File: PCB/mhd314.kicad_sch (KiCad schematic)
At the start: 35 parts, among them J1 Raspberry_Pi_2_3, J2 AudioJack_Pentaconn, J4 AudioJack3_SwitchTR, SW1 SW_Push

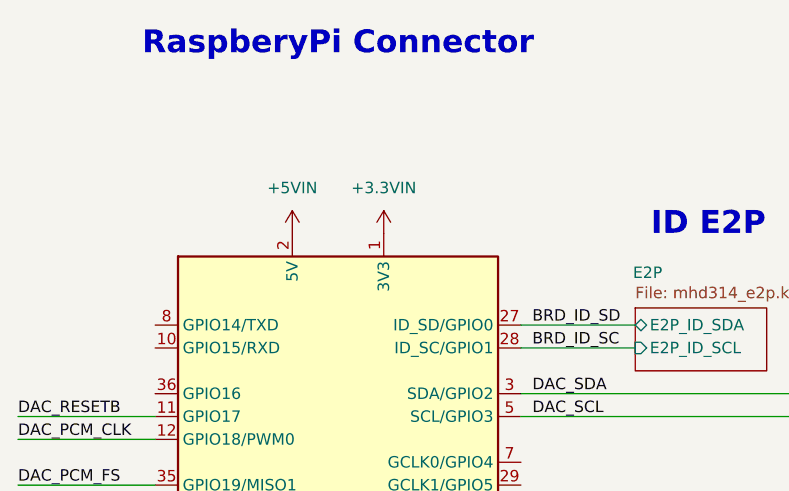
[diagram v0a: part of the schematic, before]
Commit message: Basic routing finished. Still missing some optimizing steps and DRC
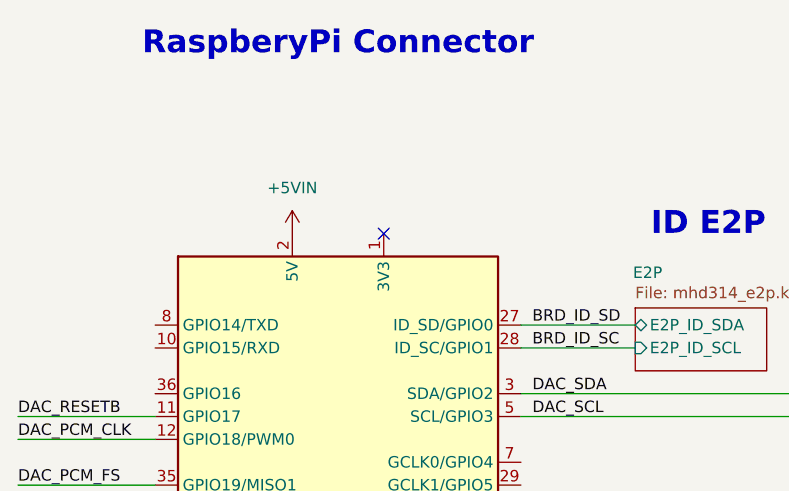
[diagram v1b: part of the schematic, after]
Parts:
- J2: footprint _mahaudio KiCad Library:Jack_4.4mm_Pentaconn_NBA1-24-001_Horizontal -> mahaudio KiCad Library:Jack_4.4mm_Pentaconn_NBA1-24-001_Horizontal; symbol mahaudio_kicad_lib:AudioJack_Pentaconn -> mahaudio KiCad Library:AudioJack_Pentaconn
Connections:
- net +3.3VIN: no longer names the net of J1.1 (3V3), J1.17 (3V3)
- no-connect marks 7 -> 8
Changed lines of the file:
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@@
 	)
 	(no_connect
+		(at 62.23 52.07)
+	)
+	(no_connect
 		(at 254 44.45)
 	)
@@
 	(symbol
 		(lib_id "power:VBUS")
-		(at 62.23 52.07 0)
-		(unit 1)
-		(exclude_from_sim no)
-		(in_bom yes)
-		(on_board yes)
-		(dnp no)
-		(fields_autoplaced yes)
-		(property "Reference" "#PWR083"
-			(at 62.23 55.88 0)
-			(effects
-				(font
-					(size 1.27 1.27)
-				)
-				(hide yes)
-			)
-		)
-		(property "Value" "+3.3VIN"
-			(at 62.23 46.99 0)
-			(effects
-				(font
-					(size 1.27 1.27)
-				)
-			)
-		)
-		(property "Footprint" ""
-			(at 62.23 52.07 0)
-			(effects
-				(font
-					(size 1.27 1.27)
-				)
-				(hide yes)
-			)
-		)
-		(property "Datasheet" ""
-			(at 62.23 52.07 0)
-			(effects
-				(font
-					(size 1.27 1.27)
-				)
-				(hide yes)
-			)
-		)
-		(property "Description" "Power symbol creates a global label with name \"VBUS\""
-			(at 62.23 52.07 0)
-			(effects
-				(font
-					(size 1.27 1.27)
-				)
-				(hide yes)
-			)
-		)
-		(pin "1"
-		)
-		(instances
-			(project "mhd314"
-				(path "/afee45fc-2361-4efb-9cde-757fc2efd57b"
-					(reference "#PWR083")
-					(unit 1)
-				)
-			)
-		)
-	)
-	(symbol
-		(lib_id "power:VBUS")
 		(at 52.07 52.07 0)
 		(unit 1)
@@
 	)
 	(symbol
-		(lib_id "mahaudio_kicad_lib:AudioJack_Pentaconn")
+		(lib_id "mahaudio KiCad Library:AudioJack_Pentaconn")
 		(at 259.08 72.39 180)
 		(unit 1)
@@
 			)
 		)
-		(property "Footprint" "_mahaudio KiCad Library:Jack_4.4mm_Pentaconn_NBA1-24-001_Horizontal"
+		(property "Footprint" "mahaudio KiCad Library:Jack_4.4mm_Pentaconn_NBA1-24-001_Horizontal"
 			(at 263.652 59.436 0)
 			(effects

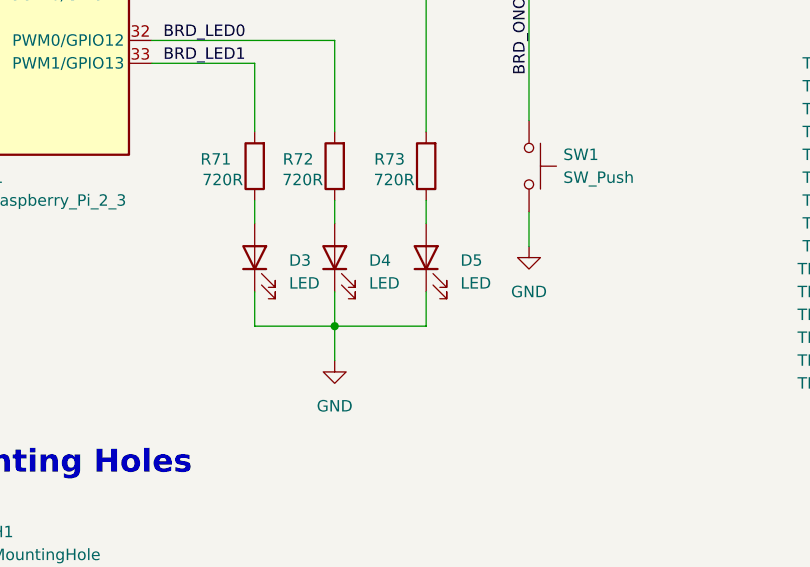
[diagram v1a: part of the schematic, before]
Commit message: Routing revised, added some missing parameters to components
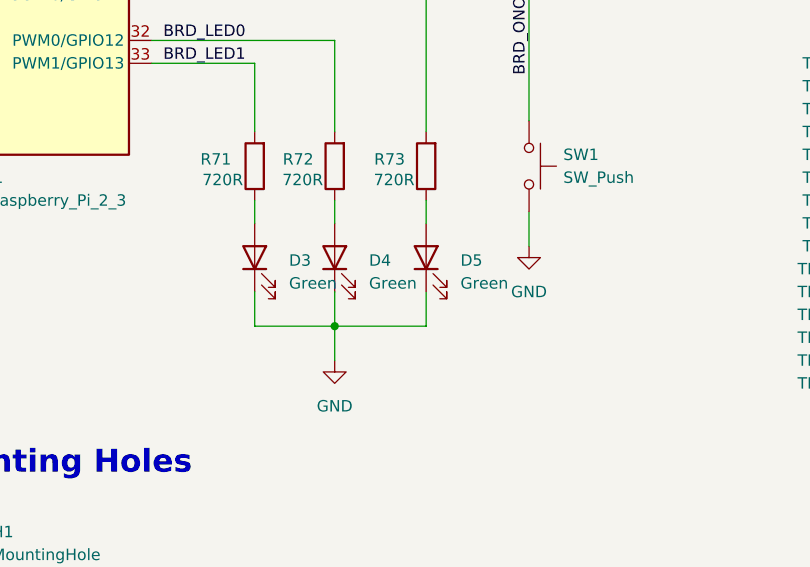
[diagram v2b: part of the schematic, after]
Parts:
- D3, D4, D5: value LED -> Green
- TP1, TP10, TP11, TP12, TP13, TP14, TP15, TP16, TP17, TP18, TP19, TP2, TP20, TP21, TP3, TP4, TP5, TP6, TP7, TP8, TP9: now left out of the parts list
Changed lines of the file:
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@@
 		(unit 1)
 		(exclude_from_sim no)
-		(in_bom yes)
+		(in_bom no)
 		(on_board yes)
 		(dnp no)
@@
 		(unit 1)
 		(exclude_from_sim no)
-		(in_bom yes)
+		(in_bom no)
 		(on_board yes)
 		(dnp no)
@@
 		(unit 1)
 		(exclude_from_sim no)
-		(in_bom yes)
+		(in_bom no)
 		(on_board yes)
 		(dnp no)
@@
 			)
 		)
-		(property "Value" "LED"
+		(property "Value" "Green"
 			(at 111.76 129.8574 90)
 			(effects
@@
 		(unit 1)
 		(exclude_from_sim no)
-		(in_bom yes)
+		(in_bom no)
 		(on_board yes)
 		(dnp no)
@@
 		(unit 1)
 		(exclude_from_sim no)
-		(in_bom yes)
+		(in_bom no)
 		(on_board yes)
 		(dnp no)
@@
 		(unit 1)
 		(exclude_from_sim no)
-		(in_bom yes)
+		(in_bom no)
 		(on_board yes)
 		(dnp no)
@@
 			)
 		)
-		(property "Datasheet" "~"
+		(property "Datasheet" "https://www.sameskydevices.com/product/resource/sj1-353xng.pdf"
 			(at 259.08 52.07 0)
 			(effects
@@
 		(unit 1)
 		(exclude_from_sim no)
-		(in_bom yes)
+		(in_bom no)
 		(on_board yes)
 		(dnp no)
@@
 		(unit 1)
 		(exclude_from_sim no)
-		(in_bom yes)
+		(in_bom no)
 		(on_board yes)
 		(dnp no)
@@
 		(unit 1)
 		(exclude_from_sim no)
-		(in_bom yes)
+		(in_bom no)
 		(on_board yes)
 		(dnp no)
@@
 		(unit 1)
 		(exclude_from_sim no)
-		(in_bom yes)
+		(in_bom no)
 		(on_board yes)
 		(dnp no)
@@
 		(unit 1)
 		(exclude_from_sim no)
-		(in_bom yes)
+		(in_bom no)
 		(on_board yes)
 		(dnp no)
@@
 		(unit 1)
 		(exclude_from_sim no)
-		(in_bom yes)
+		(in_bom no)
 		(on_board yes)
 		(dnp no)
@@
 		(unit 1)
 		(exclude_from_sim no)
-		(in_bom yes)
+		(in_bom no)
 		(on_board yes)
 		(dnp no)
@@
 			)
 		)
-		(property "Value" "LED"
+		(property "Value" "Green"
 			(at 101.6 129.8574 90)
 			(effects
@@
 		(unit 1)
 		(exclude_from_sim no)
-		(in_bom yes)
+		(in_bom no)
 		(on_board yes)
 		(dnp no)
@@
 		(unit 1)
 		(exclude_from_sim no)
-		(in_bom yes)
+		(in_bom no)
 		(on_board yes)
 		(dnp no)
@@
 		(unit 1)
 		(exclude_from_sim no)
-		(in_bom yes)
+		(in_bom no)
 		(on_board yes)
 		(dnp no)
@@
 		(unit 1)
 		(exclude_from_sim no)
-		(in_bom yes)
+		(in_bom no)
 		(on_board yes)
 		(dnp no)
@@
 		(unit 1)
 		(exclude_from_sim no)
-		(in_bom yes)
+		(in_bom no)
 		(on_board yes)
 		(dnp no)
@@
 		(unit 1)
 		(exclude_from_sim no)
-		(in_bom yes)
+		(in_bom no)
 		(on_board yes)
 		(dnp no)
@@
 		(unit 1)
 		(exclude_from_sim no)
-		(in_bom yes)
+		(in_bom no)
 		(on_board yes)
 		(dnp no)
@@
 		(unit 1)
 		(exclude_from_sim no)
-		(in_bom yes)
+		(in_bom no)
 		(on_board yes)
 		(dnp no)
@@
 			)
 		)
-		(property "Value" "LED"
+		(property "Value" "Green"
 			(at 92.71 129.8574 90)
 			(effects

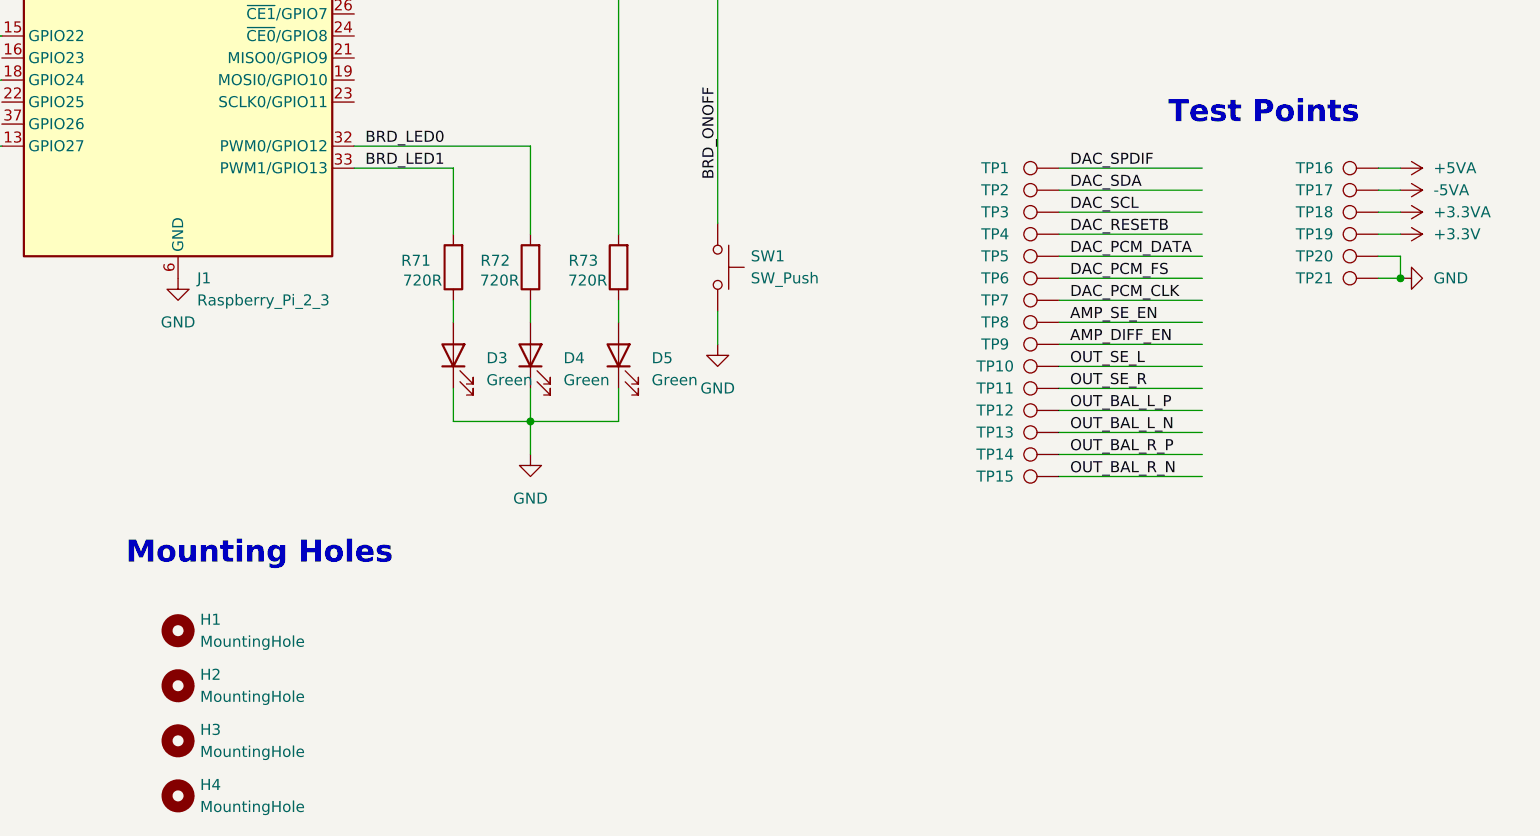
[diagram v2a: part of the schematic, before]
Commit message: Updated PCB with digital traxce suggestions. Added JLCPCB Pns
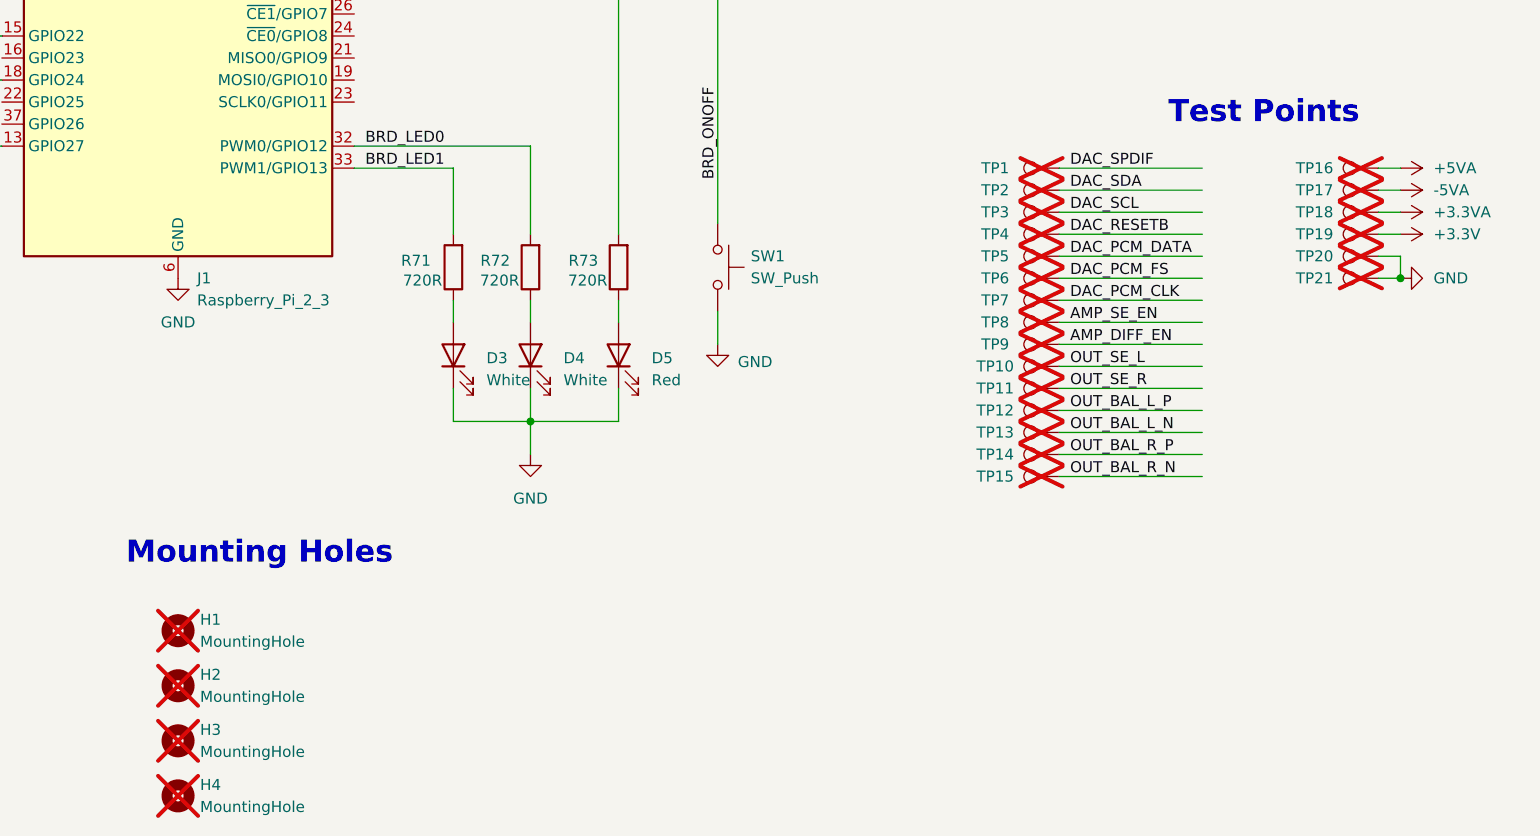
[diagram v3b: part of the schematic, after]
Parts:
- D3, D4: value Green -> White; JLCPCBPn (none) -> C2290
- D5: value Green -> Red; JLCPCBPn (none) -> C2286
- H1, H2, H3, H4, TP1, TP10, TP11, TP12, TP13, TP14, TP15, TP16, TP17, TP18, TP19, TP2, TP20, TP21, TP3, TP4, TP5, TP6, TP7, TP8, TP9: now not fitted
- J1: JLCPCBPn (none) -> C132132
- J2: JLCPCBPn (none) -> C2762984
- J4: footprint _mahaudio KiCad Library:Jack_3.5mm_CUI_SJ1-3535NG_Horizontal_3D -> mahaudio KiCad Library:Jack_3.5mm_CUI_SJ1-3535NG_Horizontal_3D; JLCPCBPn (none) -> C22359743
- R71, R72, R73: JLCPCBPn (none) -> C416571; Tolerance 5% -> 1%
- SW1: JLCPCBPn (none) -> C285519
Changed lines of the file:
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@@
 			)
 		)
-		(property "Tolerance" "5%"
+		(property "Tolerance" "1%"
+			(at 97.79 116.84 0)
+			(effects
+				(font
+					(size 1.27 1.27)
+				)
+				(hide yes)
+			)
+		)
+		(property "JLCPCBPn" "C416571"
 			(at 97.79 116.84 0)
 			(effects
@@
 		(in_bom no)
 		(on_board yes)
-		(dnp no)
+		(dnp yes)
 		(property "Reference" "TP21"
 			(at 188.214 118.11 90)
@@
 		(in_bom no)
 		(on_board yes)
-		(dnp no)
+		(dnp yes)
 		(property "Reference" "TP15"
 			(at 151.384 140.97 90)
@@
 		(in_bom no)
 		(on_board yes)
-		(dnp no)
+		(dnp yes)
 		(property "Reference" "TP8"
 			(at 151.384 123.19 90)
@@
 			)
 		)
-		(property "Tolerance" "5%"
+		(property "Tolerance" "1%"
+			(at 88.9 116.84 0)
+			(effects
+				(font
+					(size 1.27 1.27)
+				)
+				(hide yes)
+			)
+		)
+		(property "JLCPCBPn" "C416571"
 			(at 88.9 116.84 0)
 			(effects
@@
 			)
 		)
-		(property "Value" "Green"
+		(property "Value" "Red"
 			(at 111.76 129.8574 90)
 			(effects
@@
 			)
 		)
+		(property "JLCPCBPn" "C2286"
+			(at 107.95 127 0)
+			(effects
+				(font
+					(size 1.27 1.27)
+				)
+				(hide yes)
+			)
+		)
 		(pin "2"
 		)
@@
 		(in_bom no)
 		(on_board yes)
-		(dnp no)
+		(dnp yes)
 		(property "Reference" "TP12"
 			(at 151.384 133.35 90)
@@
 		(in_bom no)
 		(on_board yes)
-		(dnp no)
+		(dnp yes)
 		(fields_autoplaced yes)
 		(property "Reference" "H4"
@@
 		(in_bom no)
 		(on_board yes)
-		(dnp no)
+		(dnp yes)
 		(fields_autoplaced yes)
 		(property "Reference" "H1"
@@
 		(in_bom no)
 		(on_board yes)
-		(dnp no)
+		(dnp yes)
 		(property "Reference" "TP3"
 			(at 151.384 110.49 90)
@@
 		(in_bom no)
 		(on_board yes)
-		(dnp no)
+		(dnp yes)
 		(property "Reference" "TP1"
 			(at 151.384 105.41 90)
@@
 		(in_bom no)
 		(on_board yes)
-		(dnp no)
+		(dnp yes)
 		(fields_autoplaced yes)
 		(property "Reference" "H2"
@@
 			)
 		)
-		(property "Footprint" "_mahaudio KiCad Library:Jack_3.5mm_CUI_SJ1-3535NG_Horizontal_3D"
+		(property "Footprint" "mahaudio KiCad Library:Jack_3.5mm_CUI_SJ1-3535NG_Horizontal_3D"
 			(at 259.08 52.07 0)
 			(effects
@@
 			)
 		)
+		(property "JLCPCBPn" "C22359743"
+			(at 259.08 52.07 0)
+			(effects
+				(font
+					(size 1.27 1.27)
+				)
+				(hide yes)
+			)
+		)
 		(pin "RN"
 		)
@@
 			)
 		)
+		(property "JLCPCBPn" "C285519"
+			(at 119.38 116.84 0)
+			(effects
+				(font
+					(size 1.27 1.27)
+				)
+				(hide yes)
+			)
+		)
 		(pin "1"
 		)
@@
 		(in_bom no)
 		(on_board yes)
-		(dnp no)
+		(dnp yes)
 		(property "Reference" "TP13"
 			(at 151.384 135.89 90)
@@
 		(in_bom no)
 		(on_board yes)
-		(dnp no)
+		(dnp yes)
 		(property "Reference" "TP19"
 			(at 188.214 113.03 90)
@@
 		(in_bom no)
 		(on_board yes)
-		(dnp no)
+		(dnp yes)
 		(property "Reference" "TP7"
 			(at 151.384 120.65 90)
@@
 		(in_bom no)
 		(on_board yes)
-		(dnp no)
+		(dnp yes)
 		(property "Reference" "TP17"
 			(at 188.214 107.95 90)
@@
 		(in_bom no)
 		(on_board yes)
-		(dnp no)
+		(dnp yes)
 		(property "Reference" "TP14"
 			(at 151.384 138.43 90)
@@
 		(in_bom no)
 		(on_board yes)
-		(dnp no)
+		(dnp yes)
 		(property "Reference" "TP5"
 			(at 151.384 115.57 90)
@@
 		(in_bom no)
 		(on_board yes)
-		(dnp no)
+		(dnp yes)
 		(property "Reference" "TP10"
 			(at 151.384 128.27 90)
@@
 			)
 		)
-		(property "Tolerance" "5%"
+		(property "Tolerance" "1%"
+			(at 107.95 116.84 0)
+			(effects
+				(font
+					(size 1.27 1.27)
+				)
+				(hide yes)
+			)
+		)
+		(property "JLCPCBPn" "C416571"
 			(at 107.95 116.84 0)
 			(effects
@@
 			)
 		)
-		(property "Value" "Green"
+		(property "Value" "White"
 			(at 101.6 129.8574 90)
 			(effects
@@
 			)
 		)
+		(property "JLCPCBPn" "C2290"
+			(at 97.79 127 0)
+			(effects
+				(font
+					(size 1.27 1.27)
+				)
+				(hide yes)
+			)
+		)
 		(pin "2"
 		)
@@
 		(in_bom no)
 		(on_board yes)
-		(dnp no)
+		(dnp yes)
 		(fields_autoplaced yes)
 		(property "Reference" "H3"
@@
 		(in_bom no)
 		(on_board yes)
-		(dnp no)
+		(dnp yes)
 		(property "Reference" "TP4"
 			(at 151.384 113.03 90)
@@
 		(in_bom no)
 		(on_board yes)
-		(dnp no)
+		(dnp yes)
 		(property "Reference" "TP16"
 			(at 188.214 105.41 90)
@@
 		(in_bom no)
 		(on_board yes)
-		(dnp no)
+		(dnp yes)
 		(property "Reference" "TP6"
 			(at 151.384 118.11 90)
@@
 		(in_bom no)
 		(on_board yes)
-		(dnp no)
+		(dnp yes)
 		(property "Reference" "TP11"
 			(at 151.384 130.81 90)
@@
 		(in_bom no)
 		(on_board yes)
-		(dnp no)
+		(dnp yes)
 		(property "Reference" "TP2"
 			(at 151.384 107.95 90)
@@
 		(in_bom no)
 		(on_board yes)
-		(dnp no)
+		(dnp yes)
 		(property "Reference" "TP20"
 			(at 188.214 115.57 90)
@@
 			)
 		)
+		(property "JLCPCBPn" "C132132"
+			(at 57.15 85.09 0)
+			(effects
+				(font
+					(size 1.27 1.27)
+				)
+				(hide yes)
+			)
+		)
 		(pin "30"
 		)
@@
 		(in_bom no)
 		(on_board yes)
-		(dnp no)
+		(dnp yes)
 		(property "Reference" "TP9"
 			(at 151.384 125.73 90)
@@
 		(on_board yes)
 		(dnp no)
-		(fields_autoplaced yes)
 		(property "Reference" "#PWR0107"
 			(at 119.38 132.08 0)
@@
 		)
 		(property "Value" "GND"
-			(at 119.38 130.81 0)
+			(at 123.698 127.762 0)
 			(effects
 				(font
@@
 		(in_bom no)
 		(on_board yes)
-		(dnp no)
+		(dnp yes)
 		(property "Reference" "TP18"
 			(at 188.214 110.49 90)
@@
 			)
 		)
+		(property "JLCPCBPn" "C2762984 "
+			(at 259.08 72.39 0)
+			(effects
+				(font
+					(size 1.27 1.27)
+				)
+				(hide yes)
+			)
+		)
 		(pin "R2"
 		)
@@
 			)
 		)
-		(property "Value" "Green"
+		(property "Value" "White"
 			(at 92.71 129.8574 90)
 			(effects
@@
 			(at 88.9 127 0)
 			(effects
+				(font
+					(size 1.27 1.27)
+				)
+				(hide yes)
+			)
+		)
+		(property "JLCPCBPn" "C2290"
+			(at 88.9 127 0)
+			(effects

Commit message: Changed the 4.4mm connector and fixed a bunch o library related problems
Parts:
- J2: footprint mahaudio KiCad Library:Jack_4.4mm_Pentaconn_NBA1-24-001_Horizontal -> mahaudio KiCad Library:Jack_4.4mm_G-Switch_GT-3321667P-01_Horizontal
- J4: footprint mahaudio KiCad Library:Jack_3.5mm_CUI_SJ1-3535NG_Horizontal_3D -> Connector_Audio:Jack_3.5mm_CUI_SJ1-3535NG_Horizontal
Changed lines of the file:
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@@
 			)
 		)
-		(property "Footprint" "mahaudio KiCad Library:Jack_3.5mm_CUI_SJ1-3535NG_Horizontal_3D"
+		(property "Footprint" "Connector_Audio:Jack_3.5mm_CUI_SJ1-3535NG_Horizontal"
 			(at 259.08 52.07 0)
 			(effects
@@
 			)
 		)
-		(property "Footprint" "mahaudio KiCad Library:Jack_4.4mm_Pentaconn_NBA1-24-001_Horizontal"
+		(property "Footprint" "mahaudio KiCad Library:Jack_4.4mm_G-Switch_GT-3321667P-01_Horizontal"
 			(at 263.652 59.436 0)
 			(effects

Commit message: Added filter capacitors to OPA1622 circuitry
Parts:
- D3, D4: JLCPCBPn C2290 -> (none); LCSC Part # (none) -> C2290
- D5: JLCPCBPn C2286 -> (none); LCSC Part # (none) -> C2286
- J1: JLCPCBPn C132132 -> (none); LCSC Part # (none) -> C132132
- J2: JLCPCBPn C2762984 -> (none); LCSC Part # (none) -> C2762984
- J4: JLCPCBPn C22359743 -> (none); LCSC Part # (none) -> C22359743
- R71, R72, R73: JLCPCBPn C416571 -> (none); LCSC Part # (none) -> C416571
- SW1: JLCPCBPn C285519 -> (none); LCSC Part # (none) -> C285519
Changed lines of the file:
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@@
 			)
 		)
-		(property "JLCPCBPn" "C416571"
+		(property "LCSC Part #" "C416571"
 			(at 97.79 116.84 0)
 			(effects
@@
 			)
 		)
-		(property "JLCPCBPn" "C416571"
+		(property "LCSC Part #" "C416571"
 			(at 88.9 116.84 0)
 			(effects
@@
 			)
 		)
-		(property "JLCPCBPn" "C2286"
+		(property "LCSC Part #" "C2286"
 			(at 107.95 127 0)
 			(effects
@@
 			)
 		)
-		(property "JLCPCBPn" "C22359743"
+		(property "LCSC Part #" "C22359743"
 			(at 259.08 52.07 0)
 			(effects
@@
 			)
 		)
-		(property "JLCPCBPn" "C285519"
+		(property "LCSC Part #" "C285519"
 			(at 119.38 116.84 0)
 			(effects
@@
 			)
 		)
-		(property "JLCPCBPn" "C416571"
+		(property "LCSC Part #" "C416571"
 			(at 107.95 116.84 0)
 			(effects
@@
 			)
 		)
-		(property "JLCPCBPn" "C2290"
+		(property "LCSC Part #" "C2290"
 			(at 97.79 127 0)
 			(effects
@@
 			)
 		)
-		(property "JLCPCBPn" "C132132"
+		(property "LCSC Part #" "C132132"
 			(at 57.15 85.09 0)
 			(effects
@@
 			)
 		)
-		(property "JLCPCBPn" "C2762984 "
+		(property "LCSC Part #" "C2762984 "
 			(at 259.08 72.39 0)
 			(effects
@@
 			)
 		)
-		(property "JLCPCBPn" "C2290"
+		(property "LCSC Part #" "C2290"
 			(at 88.9 127 0)
 			(effects
